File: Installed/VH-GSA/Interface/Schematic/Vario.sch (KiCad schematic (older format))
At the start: 3 parts

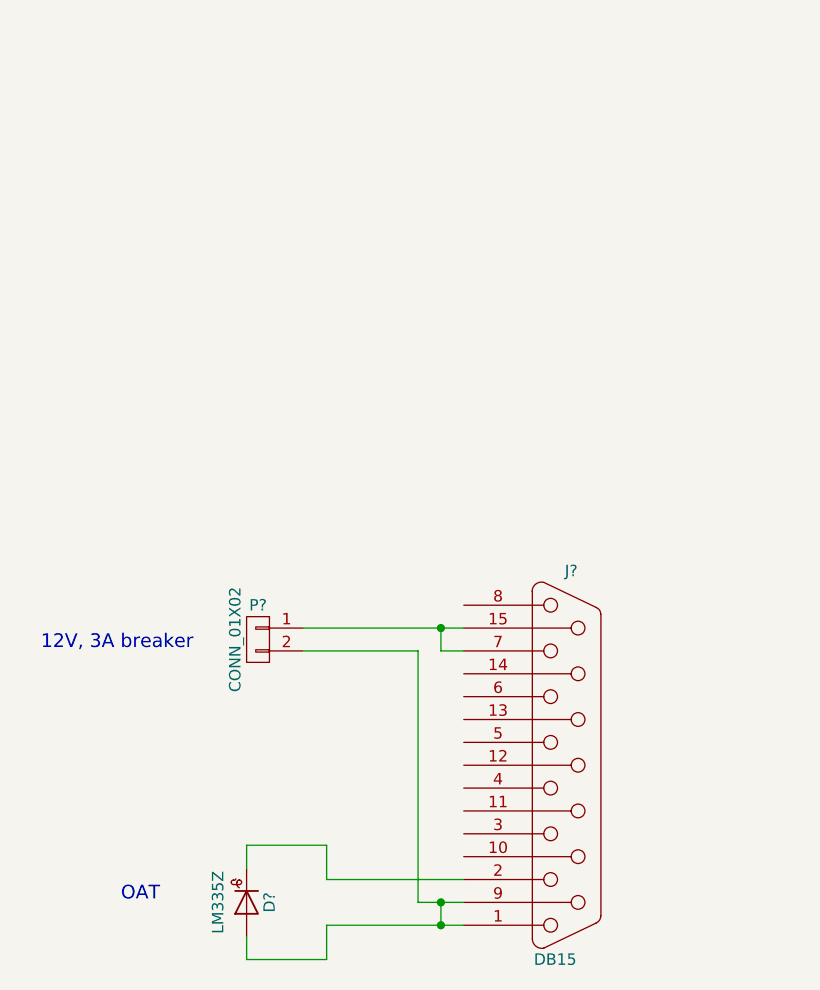
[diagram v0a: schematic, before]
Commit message: VH-GSA: Updated interface
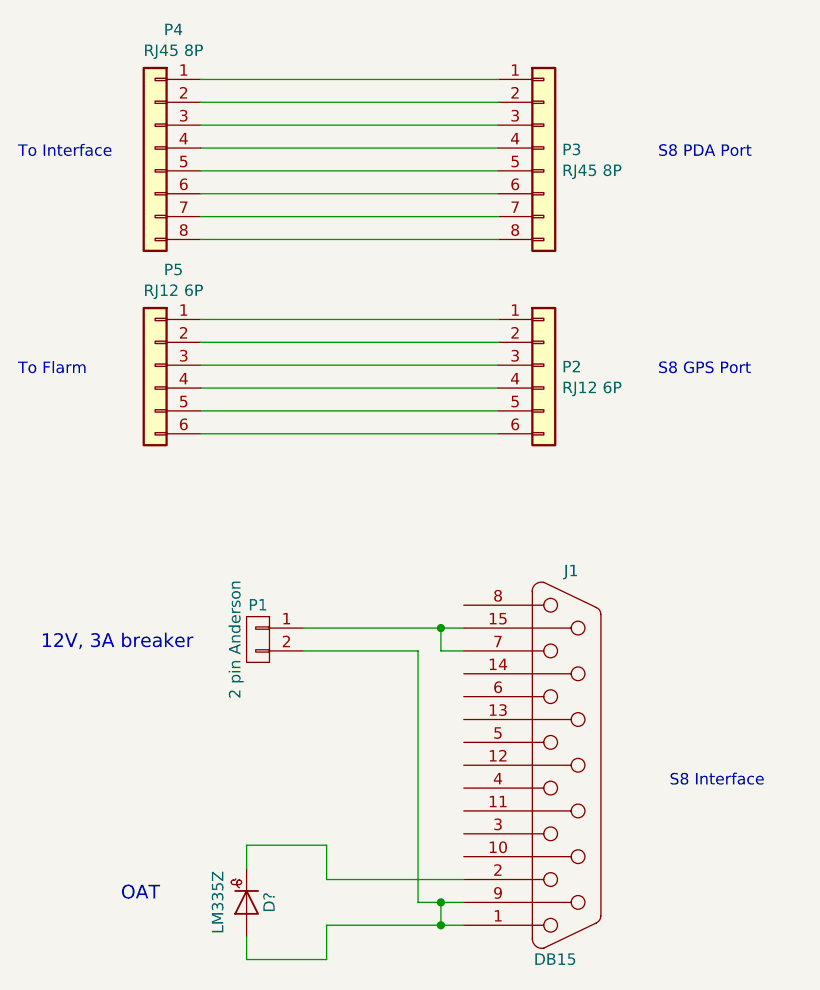
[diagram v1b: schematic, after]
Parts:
- added P2, P5: RJ12 6P, symbol Connector_Generic:Conn_01x06
- added P3, P4: RJ45 8P, symbol Connector_Generic:Conn_01x08
- P1: renamed from P?; value CONN_01X02 -> 2 pin Anderson
- gave numbers to parts that had none: 1
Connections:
- new net: P2.1 (Pin_1), P5.1 (Pin_1)
- new net: P2.2 (Pin_2), P5.2 (Pin_2)
- new net: P2.3 (Pin_3), P5.3 (Pin_3)
- new net: P2.4 (Pin_4), P5.4 (Pin_4)
- new net: P2.5 (Pin_5), P5.5 (Pin_5)
- new net: P2.6 (Pin_6), P5.6 (Pin_6)
- new net: P3.1 (Pin_1), P4.1 (Pin_1)
- new net: P3.2 (Pin_2), P4.2 (Pin_2)
- new net: P3.3 (Pin_3), P4.3 (Pin_3)
- new net: P3.4 (Pin_4), P4.4 (Pin_4)
- new net: P3.5 (Pin_5), P4.5 (Pin_5)
- new net: P3.6 (Pin_6), P4.6 (Pin_6)
- new net: P3.7 (Pin_7), P4.7 (Pin_7)
- new net: P3.8 (Pin_8), P4.8 (Pin_8)
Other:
- note added: "S8 GPS Port"
- note added: "S8 Interface"
- note added: "S8 PDA Port"
- note added: "To Flarm"
- note added: "To Interface"
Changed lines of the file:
@@
 $EndDescr
 $Comp
-L VH-GSA-rescue:DB15 J?
+L VH-GSA-rescue:DB15 J1
 U 1 1 5DCAB17A
 P 3450 3900
-F 0 "J?" H 3470 4750 50  0000 C CNN
+F 0 "J1" H 3470 4750 50  0000 C CNN
 F 1 "DB15" H 3400 3050 50  0000 C CNN
 F 2 "" H 3450 3900 50  0000 C CNN
@@
 $EndComp
 Wire Wire Line
-	2300 3300 3000 3300
+	2300 3300 2900 3300
 Wire Wire Line
 	2900 3300 2900 3400
@@
 	2900 3400 3000 3400
 Wire Wire Line
-	2800 4500 3000 4500
+	2800 4500 2900 4500
 Wire Wire Line
 	2900 4500 2900 4600
 Wire Wire Line
-	2400 4600 3000 4600
+	2400 4600 2900 4600
 $Comp
-L VH-GSA-rescue:CONN_01X02 P?
+L VH-GSA-rescue:CONN_01X02 P1
 U 1 1 5DCAB295
 P 2100 3350
-F 0 "P?" H 2100 3500 50  0000 C CNN
-F 1 "CONN_01X02" V 2200 3350 50  0000 C CNN
+F 0 "P1" H 2100 3500 50  0000 C CNN
+F 1 "2 pin Anderson" V 2200 3350 50  0000 C CNN
 F 2 "" H 2100 3350 50  0000 C CNN
 F 3 "" H 2100 3350 50  0000 C CNN
@@
 Text Notes 1500 4500 0    60   ~ 0
 OAT
+Wire Wire Line
+	2900 3300 3000 3300
+Wire Wire Line
+	2900 4500 3000 4500
+Wire Wire Line
+	2900 4600 3000 4600
+$Comp
+L Connector_Generic:Conn_01x06 P2
+U 1 1 5FC7D6E3
+P 3350 2150
+F 0 "P2" H 3430 2142 50  0000 L CNN
+F 1 "RJ12 6P" H 3430 2051 50  0000 L CNN
+F 2 "" H 3350 2150 50  0001 C CNN
+F 3 "~" H 3350 2150 50  0001 C CNN
+	1    3350 2150
+	1    0    0    -1
+$EndComp
+$Comp
+L Connector_Generic:Conn_01x08 P3
+U 1 1 5FC8118B
+P 3350 1200
+F 0 "P3" H 3430 1192 50  0000 L CNN
+F 1 "RJ45 8P" H 3430 1101 50  0000 L CNN
+F 2 "" H 3350 1200 50  0001 C CNN
+F 3 "~" H 3350 1200 50  0001 C CNN
+	1    3350 1200
+	1    0    0    -1
+$EndComp
+$Comp
+L Connector_Generic:Conn_01x08 P4
+U 1 1 5FC8122E
+P 1650 1200
+F 0 "P4" H 1570 1717 50  0000 C CNN
+F 1 "RJ45 8P" H 1570 1626 50  0000 C CNN
+F 2 "" H 1650 1200 50  0001 C CNN
+F 3 "~" H 1650 1200 50  0001 C CNN
+	1    1650 1200
+	-1   0    0    -1
+$EndComp
+Wire Wire Line
+	3150 1200 1850 1200
+Wire Wire Line
+	3150 1100 1850 1100
+Wire Wire Line
+	3150 1000 1850 1000
+Wire Wire Line
+	3150 900  1850 900
+Wire Wire Line
+	3150 1300 1850 1300
+Wire Wire Line
+	3150 1400 1850 1400
+Wire Wire Line
+	3150 1500 1850 1500
+Wire Wire Line
+	3150 1600 1850 1600
+Text Notes 1050 1250 0    50   ~ 0
+To Interface
+$Comp
+L Connector_Generic:Conn_01x06 P5
+U 1 1 5FC87271
+P 1650 2150
+F 0 "P5" H 1570 2567 50  0000 C CNN
+F 1 "RJ12 6P" H 1570 2476 50  0000 C CNN
+F 2 "" H 1650 2150 50  0001 C CNN
+F 3 "~" H 1650 2150 50  0001 C CNN
+	1    1650 2150
+	-1   0    0    -1
+$EndComp
+Wire Wire Line
+	3150 1950 1850 1950
+Wire Wire Line
+	3150 2050 1850 2050
+Wire Wire Line
+	3150 2150 1850 2150
+Wire Wire Line
+	3150 2250 1850 2250
+Wire Wire Line
+	3150 2350 1850 2350
+Wire Wire Line
+	3150 2450 1850 2450
+Text Notes 1050 2200 0    50   ~ 0
+To Flarm
+Text Notes 3850 2200 0    50   ~ 0
+S8 GPS Port
+Text Notes 3850 1250 0    50   ~ 0
+S8 PDA Port
+Text Notes 3900 4000 0    50   ~ 0
+S8 Interface
 $EndSCHEMATC
